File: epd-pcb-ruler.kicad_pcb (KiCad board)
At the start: 2 copper layers, 205 x 30 mm, 16 parts

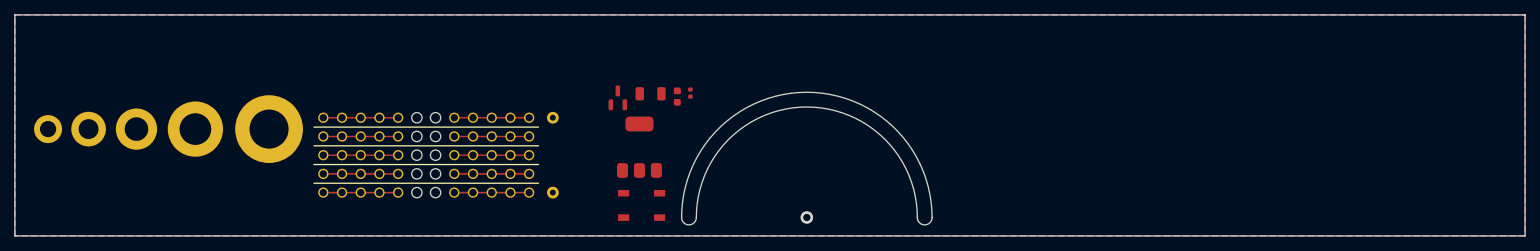
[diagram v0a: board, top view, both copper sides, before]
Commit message: Add new line art, change font, round corners
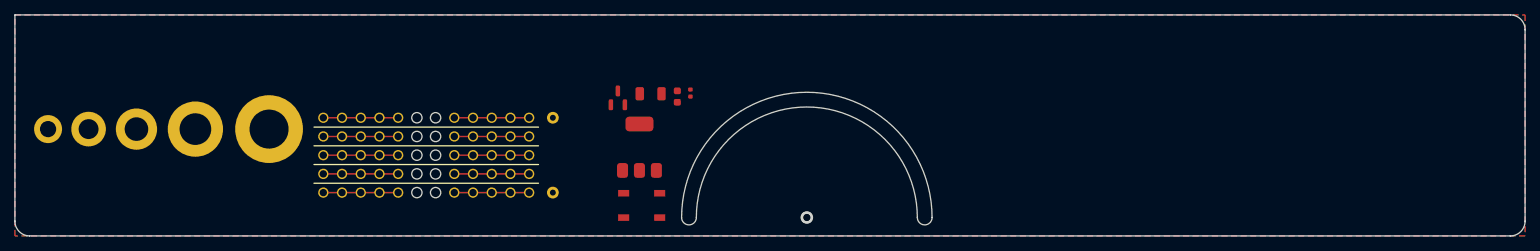
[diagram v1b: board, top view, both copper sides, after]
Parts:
- added G***: LOGO, LOGO, B.Cu at (223.0, 102.3)
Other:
- outline, holes or cut-outs redrawn
- board text added: "Design @kaine119 Artwork @harinee_b"
- board text added: "R2"
